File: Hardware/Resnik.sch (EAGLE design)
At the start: 206 parts, among them IC1 ATMEGA644M, J1 CONN_82.54_SCREW, J3 CONN_42.54_SCREW, J4 CONN_82.54_SCREW, Q1 DMG3404, Q2 DMG3404, Q3 FDN360P, Q4 FDN360P, Q5 FDN360P, Q6 DMG3404, Q7 2N7002, Q8 2N7002, U1 TLV61220DBV, U10 TPS22917DBV, U11 SN74AUP1G04YFP, U12 SN74AUP1G04YFP, U13 SN74AUP1G04YFP, U14 SN74AUP2G08DQE, U15 SN74AUP2G08DQE, U16 SN74AUP2G08DQE, U17 MIC2544MSOP, U18 MIC2544MSOP, U19 MIC2544MSOP, U2 TPS62822DLC, U20 MIC2544MSOP, U21 TPS22917DBV, U22 TPS22917DBV, U23 FT231X-Q, U24 SN74LVC1G3157DRL, U25 SN74AUP3G34DCU, U26 TXS0102DQM, U27 TXS0108RGY, U28 TXS0108RGY, U29 TXS0104RGY, U3 TPS61032RSA, U30 MCP4726A2SOT-23, U31 BME280, U32 ADS1115, U33 ADS1115, U34 INA211DCK, U35 INA210DCK, U37 TLV3691DCK, U38 TS5A21366RSE, U39 MIC94090C6, U40 SN74AHC1G86DCK, U41 MCP23018QFN, U5 BQ2980RUG, U6 TPS2105, U7 LTC4412S6, U8 TPL5111DDC, U9 TPS79733

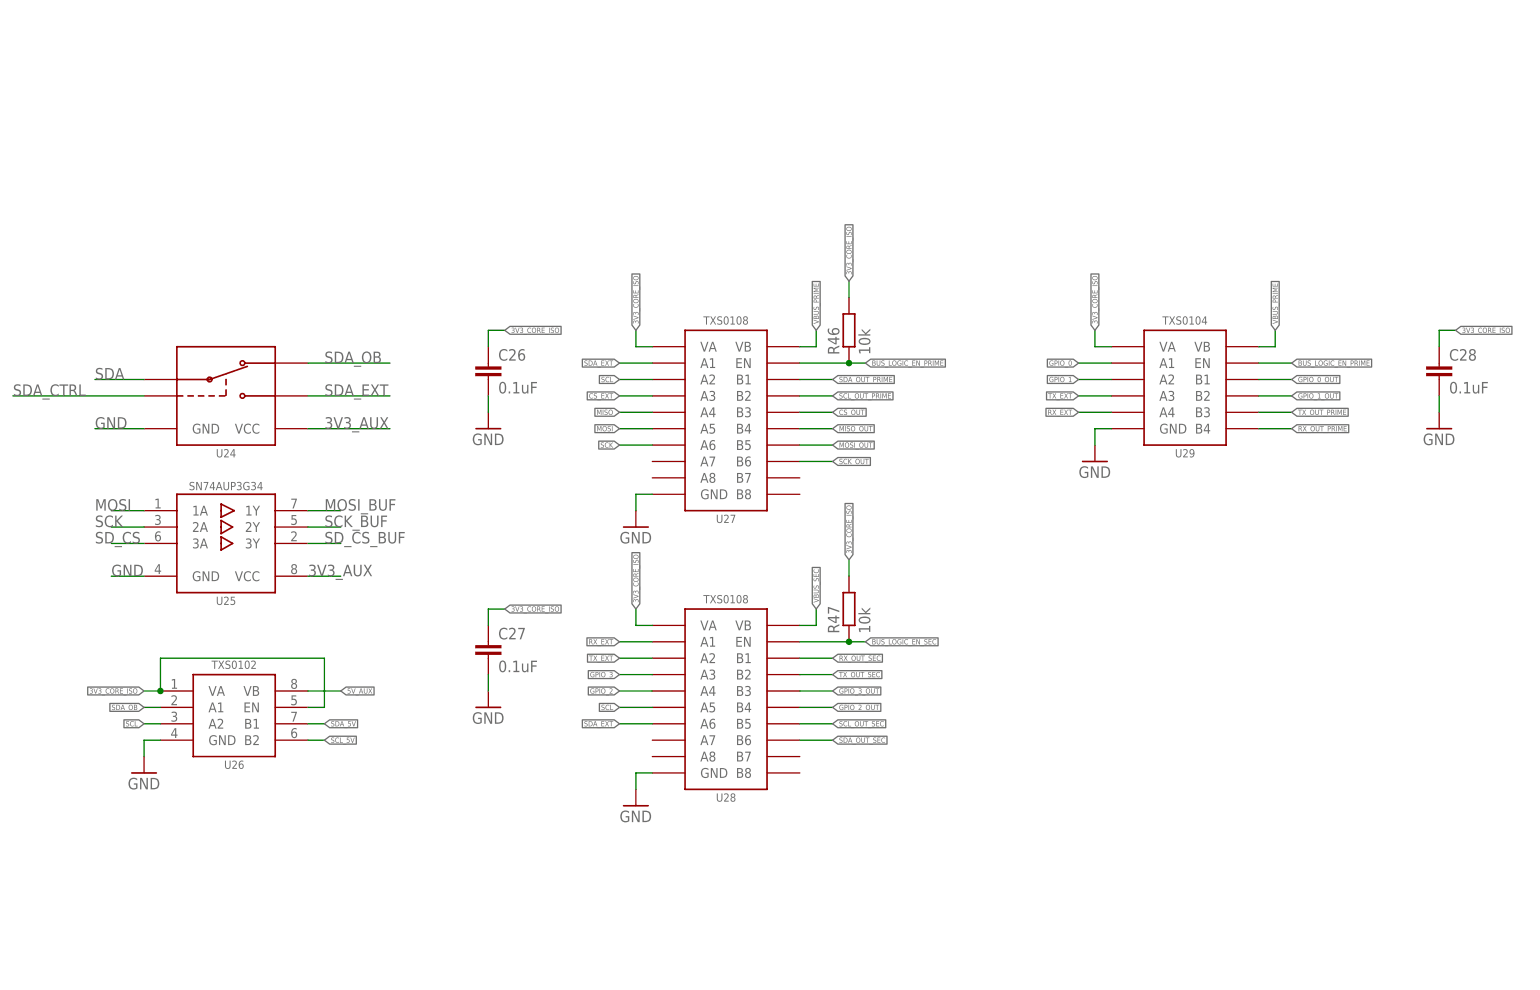
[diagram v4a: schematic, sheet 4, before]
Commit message: Hardware fixes, review and verification required, gerber generated
Gerber generated and sent to DFM, verification and review required
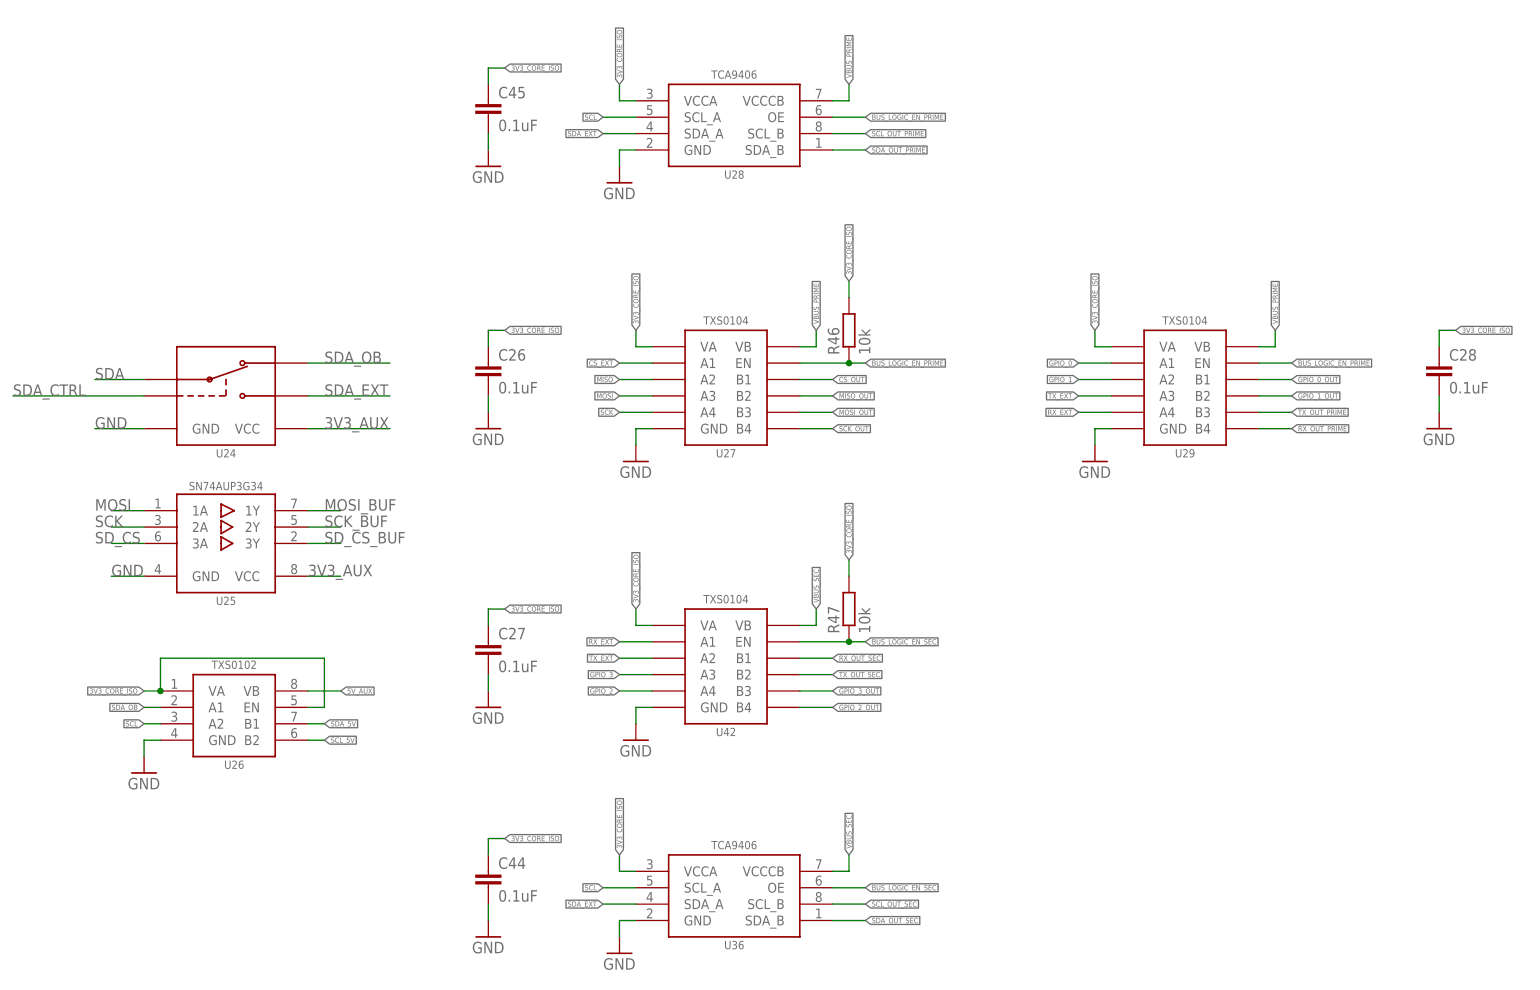
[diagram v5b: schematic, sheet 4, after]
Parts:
- added C44, C45: 0.1uF, bschulz_passives:C-EU0.1UFC0402
- added D9: (no value), bschulz:DIODEDO-214AC
- added R54: (no value), bschulz_passives:R-EU_10KR0402
- added U36: TCA9406DCU, bschulz:TCA9406DCU
- added U42: TXS0104RGY, bschulz:TXS0104RGY
- Q4: value FDN360P -> 2N7002; device bschulz:MOSFET_PCH-FDN360P -> bschulz:MOSFET-NCH-2N7002PW
- U27: value TXS0108RGY -> TXS0104RGY; device bschulz:TXS0108RGY -> bschulz:TXS0104RGY
- U28: value TXS0108RGY -> TCA9406DCU; device bschulz:TXS0108RGY -> bschulz:TCA9406DCU
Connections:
- new net RST_TRIG: MS1.GPIO9, Q4.G, R54.2
- net 3V3_CORE_ISO: now also C44.1, C45.1, U28.VCCA, U36.VCCA, U42.VA; no longer U28.VA
- net ADC_0: now also J1.8, U33.AIN0; no longer J2.1, JP6.1, U33.AIN1
- net ADC_1: now also J2.1, JP6.1, U33.AIN1; no longer J1.8, U33.AIN0
- net BUS_LOGIC_EN_PRIME: now also U28.OE
- net BUS_LOGIC_EN_SEC: now also U36.OE, U42.EN; no longer U28.EN
- net CS_EXT: now also U27.A1; no longer U27.A3
- net CS_OUT: now also U27.B1; no longer U27.B3
- net GND: now also C44.2, C45.2, Q4.S, R54.1, U36.GND, U42.GND
- net GPIO_2: now also U42.A4; no longer U28.A4
- net GPIO_2_OUT: now also U42.B4; no longer U28.B4
- net GPIO_3: now also U42.A3; no longer U28.A3
- net GPIO_3_OUT: now also U42.B3; no longer U28.B3
- net MISO: now also U27.A2; no longer U27.A4
- net MISO_OUT: now also U27.B2; no longer U27.B4
- net MOSI: now also U27.A3; no longer U27.A5
- net MOSI_OUT: now also U27.B3; no longer U27.B5
- net N$46: no longer Q4.G
- net RST: now also Q4.D; no longer MS1.GPIO9
- net RX_EXT: now also U42.A1; no longer U28.A1
- net RX_OUT_SEC: now also U42.B1; no longer U28.B1
- net SCK: now also U27.A4; no longer U27.A6
- net SCK_OUT: now also U27.B4; no longer U27.B6
- net SCL: now also U28.SCL_A, U36.SCL_A; no longer U27.A2, U28.A5
- net SCL_OUT_PRIME: now also U28.SCL_B; no longer U27.B2
- net SCL_OUT_SEC: now also U36.SCL_B; no longer U28.B5
- net SDA_EXT: now also U28.SDA_A, U36.SDA_A; no longer U27.A1, U28.A6
- net SDA_OUT_PRIME: now also U28.SDA_B; no longer U27.B1
- net SDA_OUT_SEC: now also U36.SDA_B; no longer U28.B6
- net TX_EXT: now also U42.A2; no longer U28.A2
- net TX_OUT_SEC: now also U42.B2; no longer U28.B2
- net VBUS_PRIME: now also U28.VCCCB
- net VBUS_SEC: now also U36.VCCCB, U42.VB; no longer U28.VB
- net VUSB_POWER: now also D9.A; no longer Q4.D
- net V_BETA: now also D9.C; no longer Q4.S

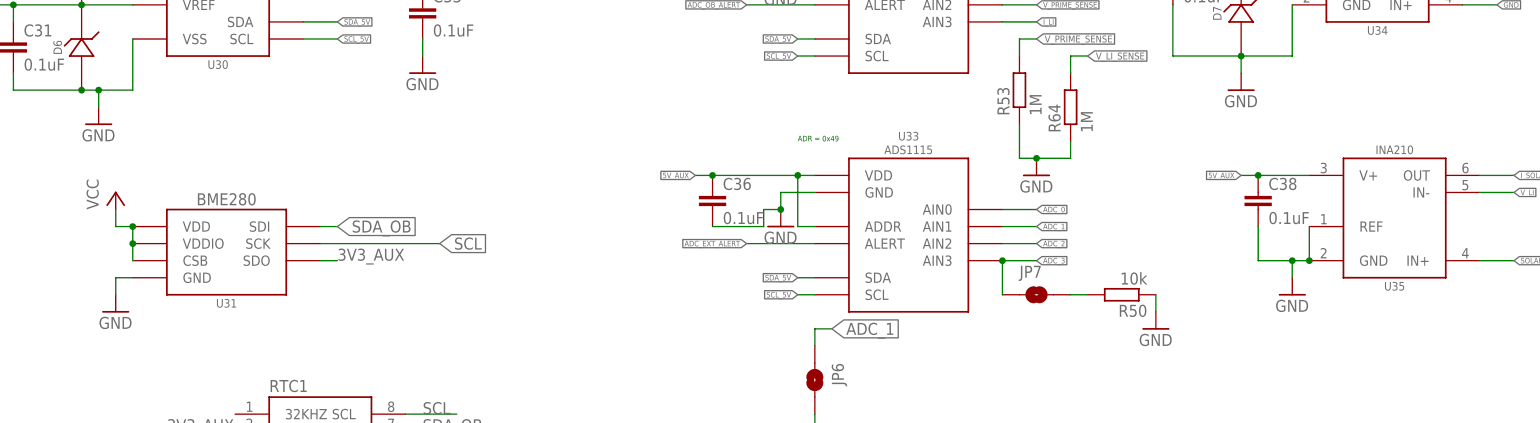
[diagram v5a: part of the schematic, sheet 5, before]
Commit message: Minor value changes, generated BoM for quote generation
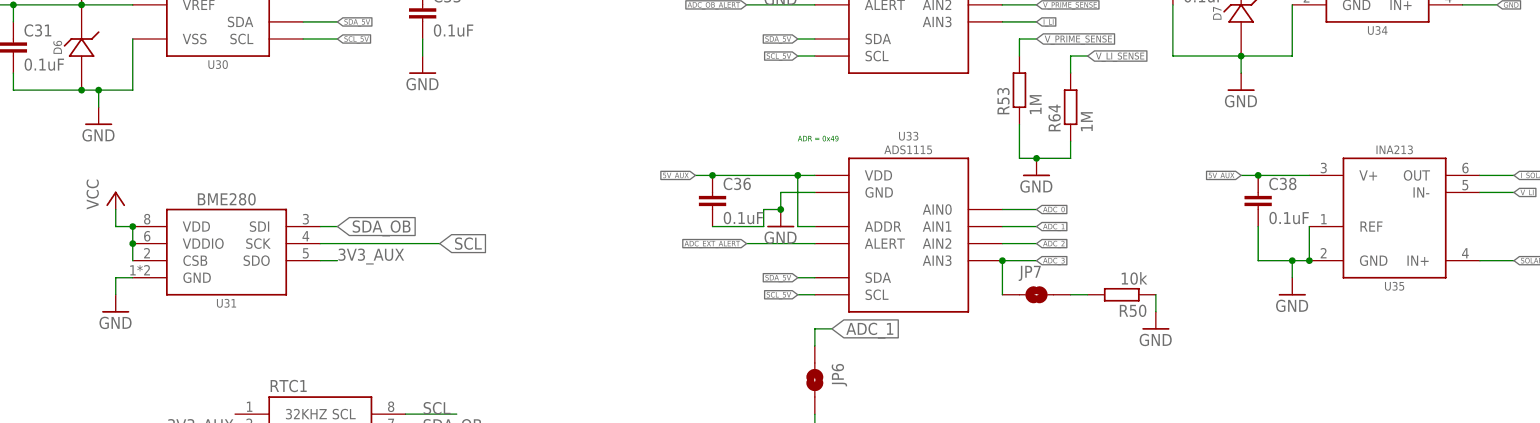
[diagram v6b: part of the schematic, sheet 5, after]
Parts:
- IC1: value ATMEGA644M -> ATMEGA1284M; device bschulz:ATMEGA644M -> bschulz:ATMEGA1284M
- R12: device bschulz_passives:R-EU_R0402 -> bschulz_passives:R-EU_1KR0402
- R22: device bschulz_passives:R-EU_R0603 -> bschulz_passives:R-EU_143KR0603
- R51: device bschulz_passives:R-EU_R0603 -> bschulz_passives:R-EU_20KR0603
- R55, R56, R59: device bschulz_passives:R-EU_R0402 -> bschulz_passives:R-EU_1MR0402
- R57, R58, R60, R61: device bschulz_passives:R-EU_R0402 -> bschulz_passives:R-EU_100KR0402
- R69: device bschulz_passives:R-EU_R0603 -> bschulz_passives:R-EU_100KR0603
- R70: device bschulz_passives:R-EU_R0603 -> bschulz_passives:R-EU_200KR0603
- R71: device bschulz_passives:R-EU_R0603 -> bschulz_passives:R-EU_1MR0603
- S5: DIGIKEY (none) -> P19888CT-ND; MF (none) -> Panasonic; MPN (none) -> EVP-BB2A9B000
- U35: value INA210DCK -> INA213DCK; device bschulz:INA210DCK -> bschulz:INA213DCK
- U39: value MIC94090C6 -> MIC94094C6; device bschulz:MIC94090C6 -> bschulz:MIC94094C6
